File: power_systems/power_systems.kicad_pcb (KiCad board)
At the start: 2 copper layers, 81 x 47 mm, 13 parts, among them J1 Screw_Terminal_01x02, J2 Screw_Terminal_01x02, J3 Screw_Terminal_01x02, U1 LM2576HVS-5, U2 LM2576HVS-12

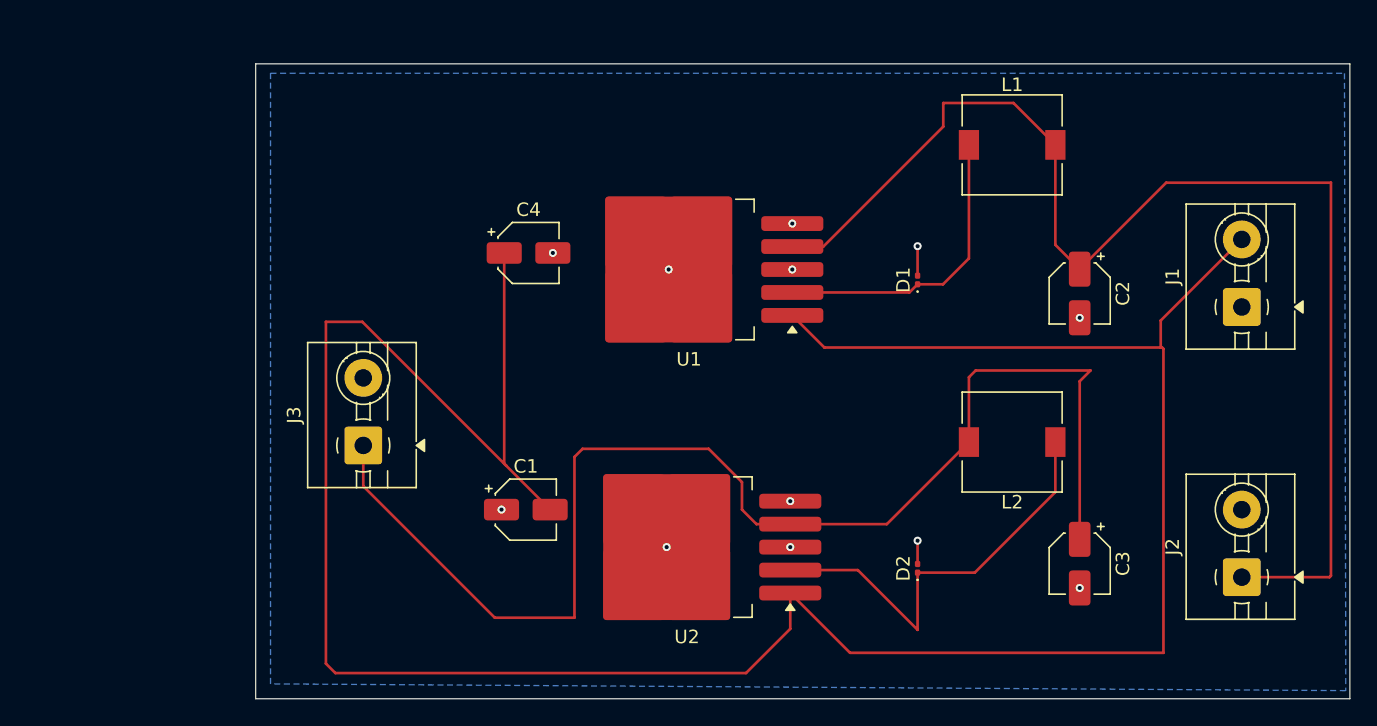
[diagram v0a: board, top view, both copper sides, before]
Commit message: Silkscreen + Rearranged components for board
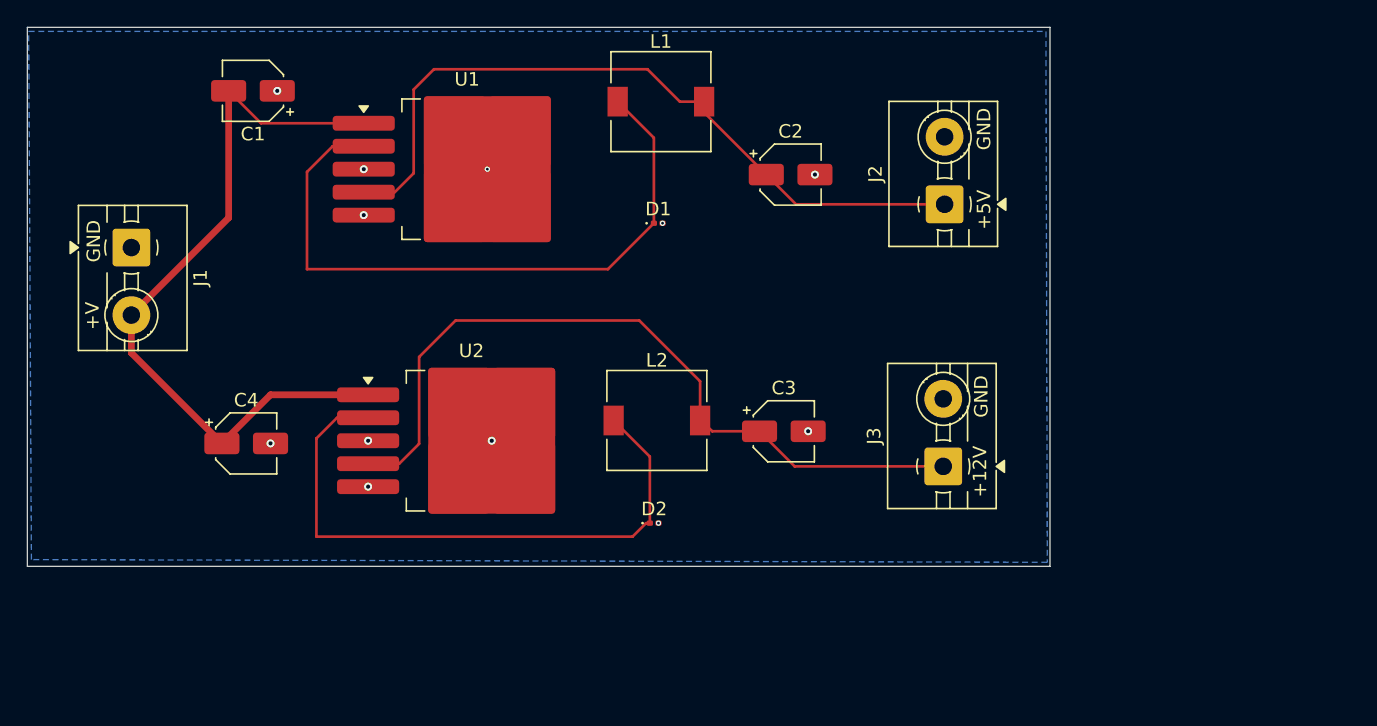
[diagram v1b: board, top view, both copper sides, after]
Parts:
- moved J1 82.3 mm to (29.8, 52.6), turned to -90 degrees
- moved J3 43.0 mm to (89.9, 68.8)
- moved C1 37.0 mm to (38.8, 41.0), turned to 180 degrees
- moved J2 35.3 mm to (90.0, 49.4)
- moved L2 26.3 mm to (68.7, 65.4), turned to 0 degrees
- moved L1 26.2 mm to (69.0, 41.8)
- moved C4 25.2 mm to (38.3, 67.1)
- moved C3 24.0 mm to (78.1, 66.2), turned to 0 degrees
- moved C2 23.1 mm to (78.6, 47.2), turned to 0 degrees
- moved D2 19.8 mm to (68.5, 73.0), turned to 0 degrees
- moved D1 19.7 mm to (68.8, 50.8), turned to 0 degrees
- moved U1 18.0 mm to (54.6, 46.8), turned to 0 degrees
- moved U2 17.8 mm to (55.0, 66.9), turned to 0 degrees
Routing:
- net Net-(J1-Pin_2): track 193.1 -> 55.2 mm
- net Net-(J3-Pin_1): track 96.9 -> 56.9 mm
- net Net-(J2-Pin_1): track 93.1 -> 55.0 mm
- net Net-(D1-K): track 22.5 -> 49.4 mm
- net Net-(D2-K): track 32.1 -> 45.5 mm
- net GND: track 3.91 -> 0.00 mm
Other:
- board size 81 x 47 mm -> 75.7 x 39.9 mm
- board text added: "+12V"
- board text added: "+5V"
- board text added: "+V"
- board text added: "GND"
